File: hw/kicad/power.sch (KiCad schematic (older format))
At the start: 1 part

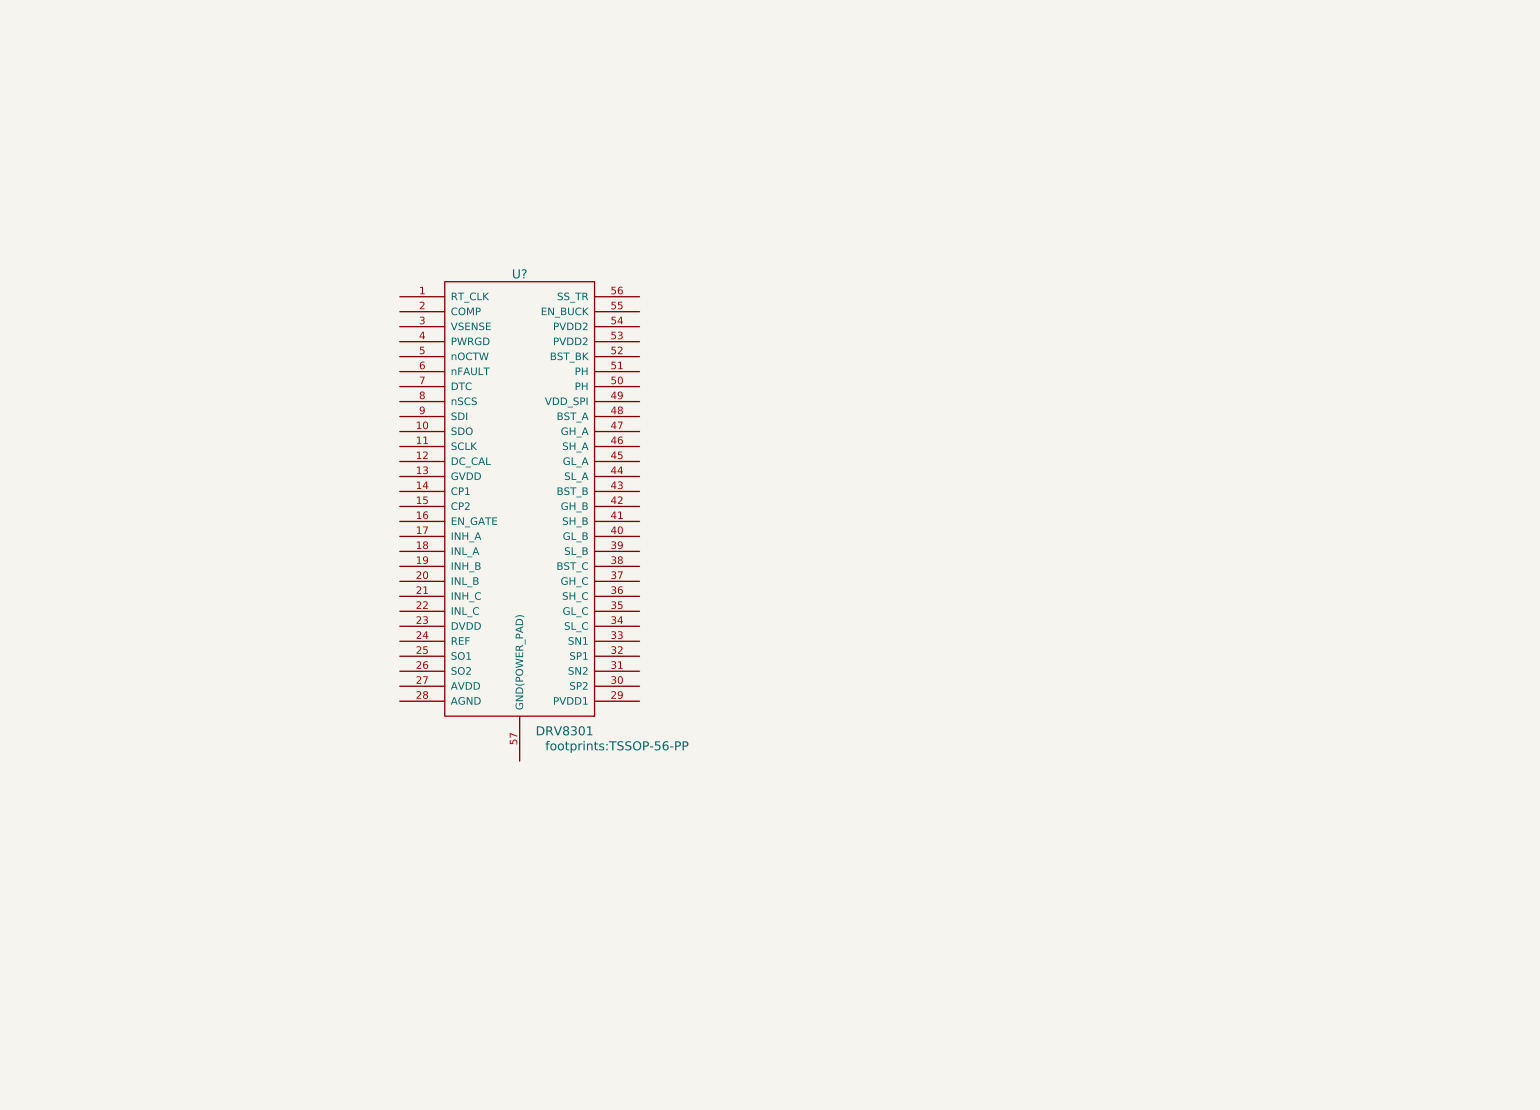
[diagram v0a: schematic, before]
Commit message: First steps on gate driver circuit
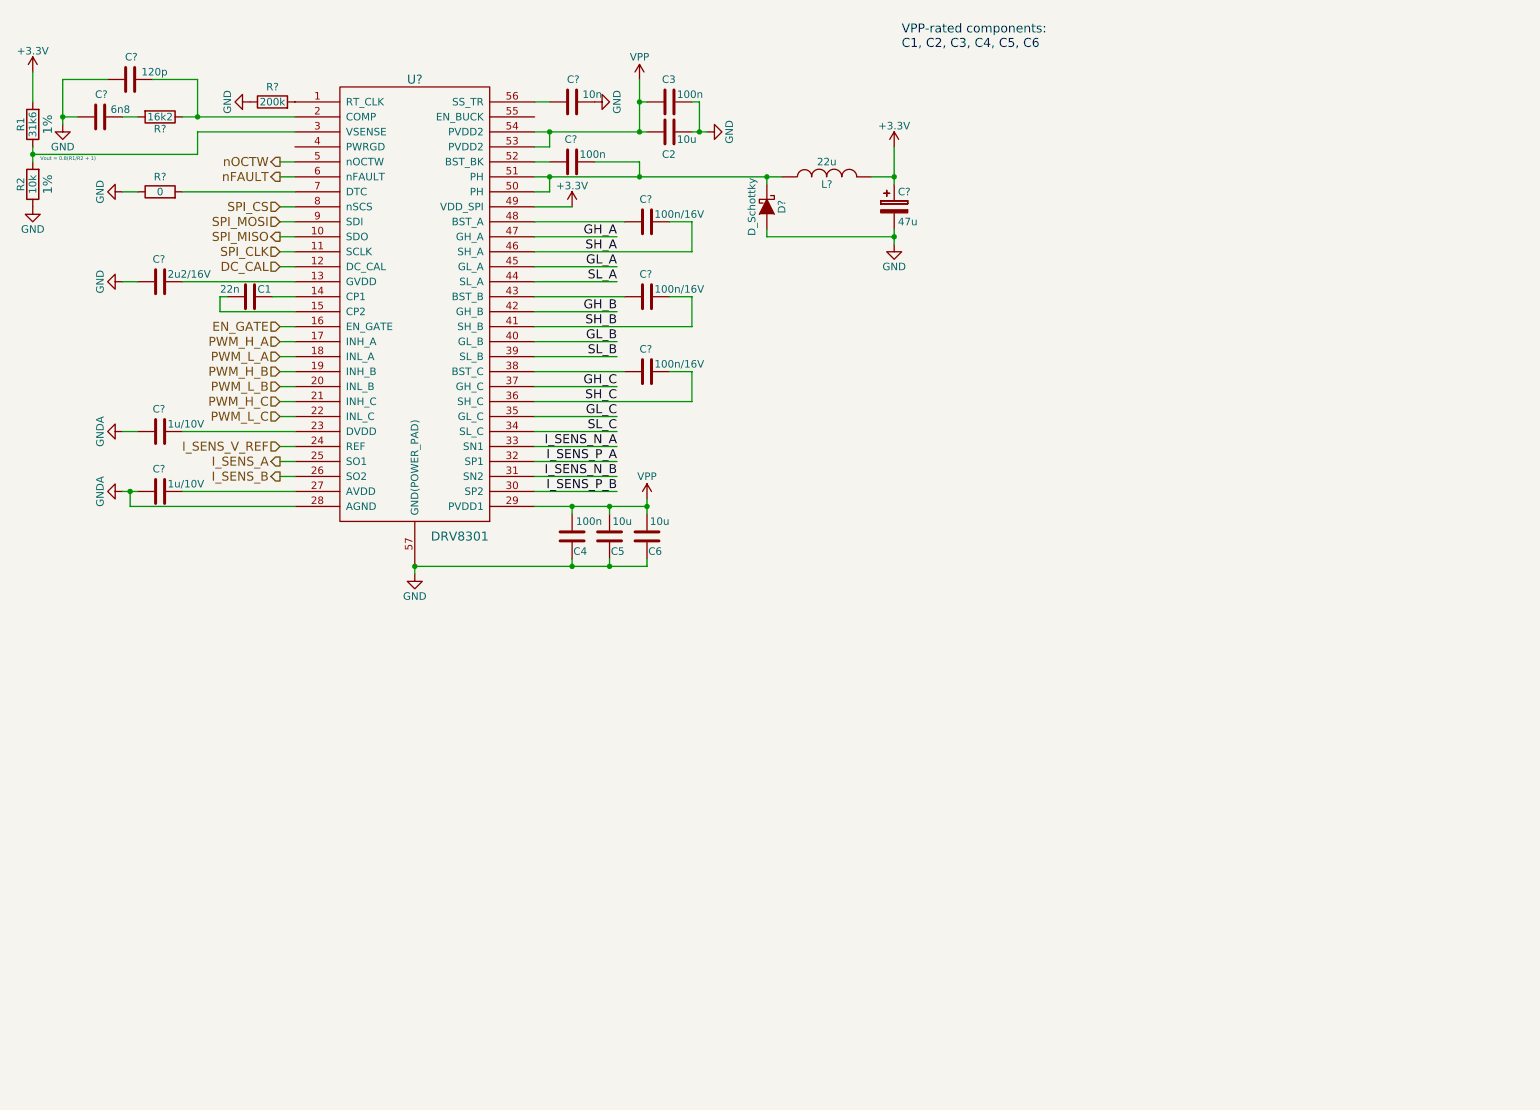
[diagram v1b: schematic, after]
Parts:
- added C1: 22n, symbol C
- added C2, C5, C6: 10u, symbol C
- added C3, C4, C?: 100n, symbol C
- added C?: 10n, symbol C
- added C?: 47u, symbol CP
- added C?: 120p, symbol C
- added C?: 6n8, symbol C
- added C?: 2u2/16V, symbol C
- added C? (x2): 1u/10V, symbol C
- added C? (x3): 100n/16V, symbol C
- added D?: D_Schottky, symbol D_Schottky
- added L?: 22u, symbol INDUCTOR
- added R1: 31k6, symbol R
- added R2: 10k, symbol R
- added R?: 200k, symbol R
- added R?: 16k2, symbol R
- added R?: 0, symbol R
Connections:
- net at U?.1 (RT_CLK): now also R?.2
- net SPI_MISO: now reaches U?.10 (SDO)
- net SPI_CLK: now reaches U?.11 (SCLK)
- net DC_CAL: now reaches U?.12 (DC_CAL)
- net at U?.13 (GVDD): now also C?.1
- net at U?.14 (CP1): now also C1.1
- net at U?.15 (CP2): now also C1.2
- net EN_GATE: now reaches U?.16 (EN_GATE)
- net PWM_H_A: now reaches U?.17 (INH_A)
- net PWM_L_A: now reaches U?.18 (INL_A)
- net PWM_H_B: now reaches U?.19 (INH_B)
- net at U?.2 (COMP): now also C?.2, R?.1
- net PWM_L_B: now reaches U?.20 (INL_B)
- net PWM_H_C: now reaches U?.21 (INH_C)
- net PWM_L_C: now reaches U?.22 (INL_C)
- net at U?.23 (DVDD): now also C?.1
- net I_SENS_V_REF: now reaches U?.24 (REF)
- net I_SENS_A: now reaches U?.25 (SO1)
- net I_SENS_B: now reaches U?.26 (SO2)
- net at U?.27 (AVDD): now also C?.1
- net GNDA: now reaches U?.28 (AGND)
- net GNDA: now also C?.2, C?.2
- net VPP: now reaches U?.29 (PVDD1)
- net VPP: now also U?.53 (PVDD2), U?.54 (PVDD2), C2.2, C3.2, C4.2, C5.2, C6.2
- net at U?.3 (VSENSE): now also R1.1, R2.2
- net I_SENS_P_B: now reaches U?.30 (SP2)
- net I_SENS_N_B: now reaches U?.31 (SN2)
- net I_SENS_P_A: now reaches U?.32 (SP1)
- net I_SENS_N_A: now reaches U?.33 (SN1)
- net SL_C: now reaches U?.34 (SL_C)
- net GL_C: now reaches U?.35 (GL_C)
- net SH_C: now reaches U?.36 (SH_C)
- net SH_C: now also C?.1
- net GH_C: now reaches U?.37 (GH_C)
- net at U?.38 (BST_C): now also C?.2
- net SL_B: now reaches U?.39 (SL_B)
- net GL_B: now reaches U?.40 (GL_B)
- net SH_B: now reaches U?.41 (SH_B)
- net SH_B: now also C?.1
- net GH_B: now reaches U?.42 (GH_B)
- net at U?.43 (BST_B): now also C?.2
- net SL_A: now reaches U?.44 (SL_A)
- net GL_A: now reaches U?.45 (GL_A)
- net SH_A: now reaches U?.46 (SH_A)
- net SH_A: now also C?.1
- net GH_A: now reaches U?.47 (GH_A)
- net at U?.48 (BST_A): now also C?.2
- net +3V3: now reaches U?.49 (VDD_SPI)
- net +3V3: now also C?.1, L?.2, R1.2
- net nOCTW: now reaches U?.5 (nOCTW)
- net at U?.50 (PH): now also U?.51 (PH), C?.1, D?.1 (K), L?.1
- net at U?.52 (BST_BK): now also C?.2
- net at U?.56 (SS_TR): now also C?.1
- net GND: now reaches U?.57 (GND(POWER_PAD))
- net GND: now also C2.1, C3.1, C4.1, C5.1, C6.1, C?.1, C?.1, C?.2, C?.2, C?.2, D?.2 (A), R2.1, R?.1, R?.1
- net nFAULT: now reaches U?.6 (nFAULT)
- net at U?.7 (DTC): now also R?.2
- net SPI_CS: now reaches U?.8 (nSCS)
- net SPI_MOSI: now reaches U?.9 (SDI)
- new net: C?.2, R?.2
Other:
- note added: "VPP-rated components:\nC1, C2, C3, C4, C5, C6"
- note added: "Vout = 0.8(R1/R2 + 1)"
- moved on the sheet: U?

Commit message: Added power mosfet footprint
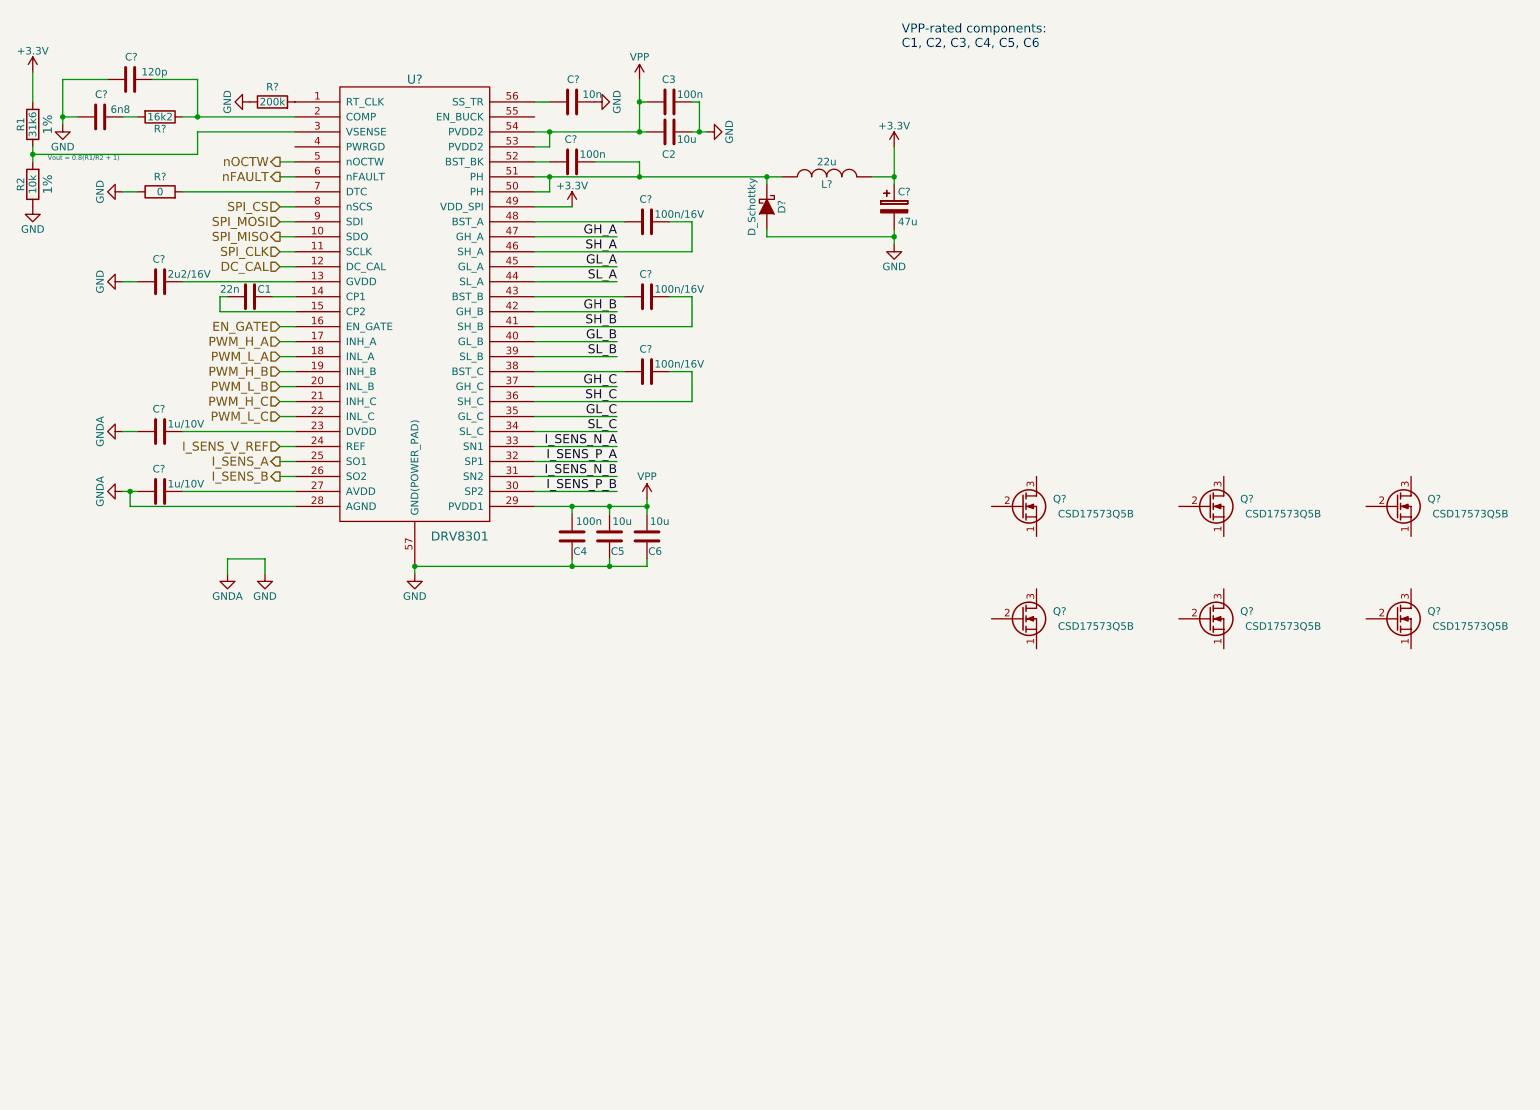
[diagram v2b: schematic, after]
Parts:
- added Q? (x6): CSD17573Q5B, SON_8_5x6:SON_8_5x6, symbol Q_NMOS_SGD
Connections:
- net GNDA is gone; now on net GND: C?.2, C?.2, U?.28 (AGND)
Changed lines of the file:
@@
 	1    0    0    -1
 $EndComp
-Text Notes 950  1500 0    24   ~ 0
+Text Notes 1000 1500 0    31   ~ 0
 Vout = 0.8(R1/R2 + 1)
 $Comp
@@
 Wire Wire Line
 	2650 3600 2550 3600
+$Comp
+L GNDA #PWR?
+U 1 1 581BA227
+P 2200 4250
+F 0 "#PWR?" H 2200 4000 50  0001 C CNN
+F 1 "GNDA" H 2200 4100 50  0000 C CNN
+F 2 "" H 2200 4250 60  0000 C CNN
+F 3 "" H 2200 4250 60  0000 C CNN
+	1    2200 4250
+	1    0    0    -1
+$EndComp
+$Comp
+L GND #PWR?
+U 1 1 581BA296
+P 2450 4250
+F 0 "#PWR?" H 2450 4000 50  0001 C CNN
+F 1 "GND" H 2450 4100 50  0000 C CNN
+F 2 "" H 2450 4250 60  0000 C CNN
+F 3 "" H 2450 4250 60  0000 C CNN
+	1    2450 4250
+	1    0    0    -1
+$EndComp
+Wire Wire Line
+	2450 4250 2450 4150
+Wire Wire Line
+	2450 4150 2200 4150
+Wire Wire Line
+	2200 4150 2200 4250
+$Comp
+L Q_NMOS_SGD Q?
+U 1 1 581CC953
+P 7500 3800
+F 0 "Q?" H 7800 3850 50  0000 R CNN
+F 1 "CSD17573Q5B" H 8250 3750 50  0000 R CNN
+F 2 "SON_8_5x6:SON_8_5x6" H 7700 3900 29  0001 C CNN
+F 3 "" H 7500 3800 60  0000 C CNN
+	1    7500 3800
+	1    0    0    -1
+$EndComp
+$Comp
+L Q_NMOS_SGD Q?
+U 1 1 581CD36C
+P 7500 4550
+F 0 "Q?" H 7800 4600 50  0000 R CNN
+F 1 "CSD17573Q5B" H 8250 4500 50  0000 R CNN
+F 2 "SON_8_5x6:SON_8_5x6" H 7700 4650 29  0001 C CNN
+F 3 "" H 7500 4550 60  0000 C CNN
+	1    7500 4550
+	1    0    0    -1
+$EndComp
+$Comp
+L Q_NMOS_SGD Q?
+U 1 1 581CD3DC
+P 8750 3800
+F 0 "Q?" H 9050 3850 50  0000 R CNN
+F 1 "CSD17573Q5B" H 9500 3750 50  0000 R CNN
+F 2 "SON_8_5x6:SON_8_5x6" H 8950 3900 29  0001 C CNN
+F 3 "" H 8750 3800 60  0000 C CNN
+	1    8750 3800
+	1    0    0    -1
+$EndComp
+$Comp
+L Q_NMOS_SGD Q?
+U 1 1 581CD456
+P 8750 4550
+F 0 "Q?" H 9050 4600 50  0000 R CNN
+F 1 "CSD17573Q5B" H 9500 4500 50  0000 R CNN
+F 2 "SON_8_5x6:SON_8_5x6" H 8950 4650 29  0001 C CNN
+F 3 "" H 8750 4550 60  0000 C CNN
+	1    8750 4550
+	1    0    0    -1
+$EndComp
+$Comp
+L Q_NMOS_SGD Q?
+U 1 1 581CD59A
+P 10000 3800
+F 0 "Q?" H 10300 3850 50  0000 R CNN
+F 1 "CSD17573Q5B" H 10750 3750 50  0000 R CNN
+F 2 "SON_8_5x6:SON_8_5x6" H 10200 3900 29  0001 C CNN
+F 3 "" H 10000 3800 60  0000 C CNN
+	1    10000 3800
+	1    0    0    -1
+$EndComp
+$Comp
+L Q_NMOS_SGD Q?
+U 1 1 581CD612
+P 10000 4550
+F 0 "Q?" H 10300 4600 50  0000 R CNN
+F 1 "CSD17573Q5B" H 10750 4500 50  0000 R CNN
+F 2 "SON_8_5x6:SON_8_5x6" H 10200 4650 29  0001 C CNN
+F 3 "" H 10000 4550 60  0000 C CNN
+	1    10000 4550
+	1    0    0    -1
+$EndComp
 $EndSCHEMATC

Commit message: Some more work on the FET-stage
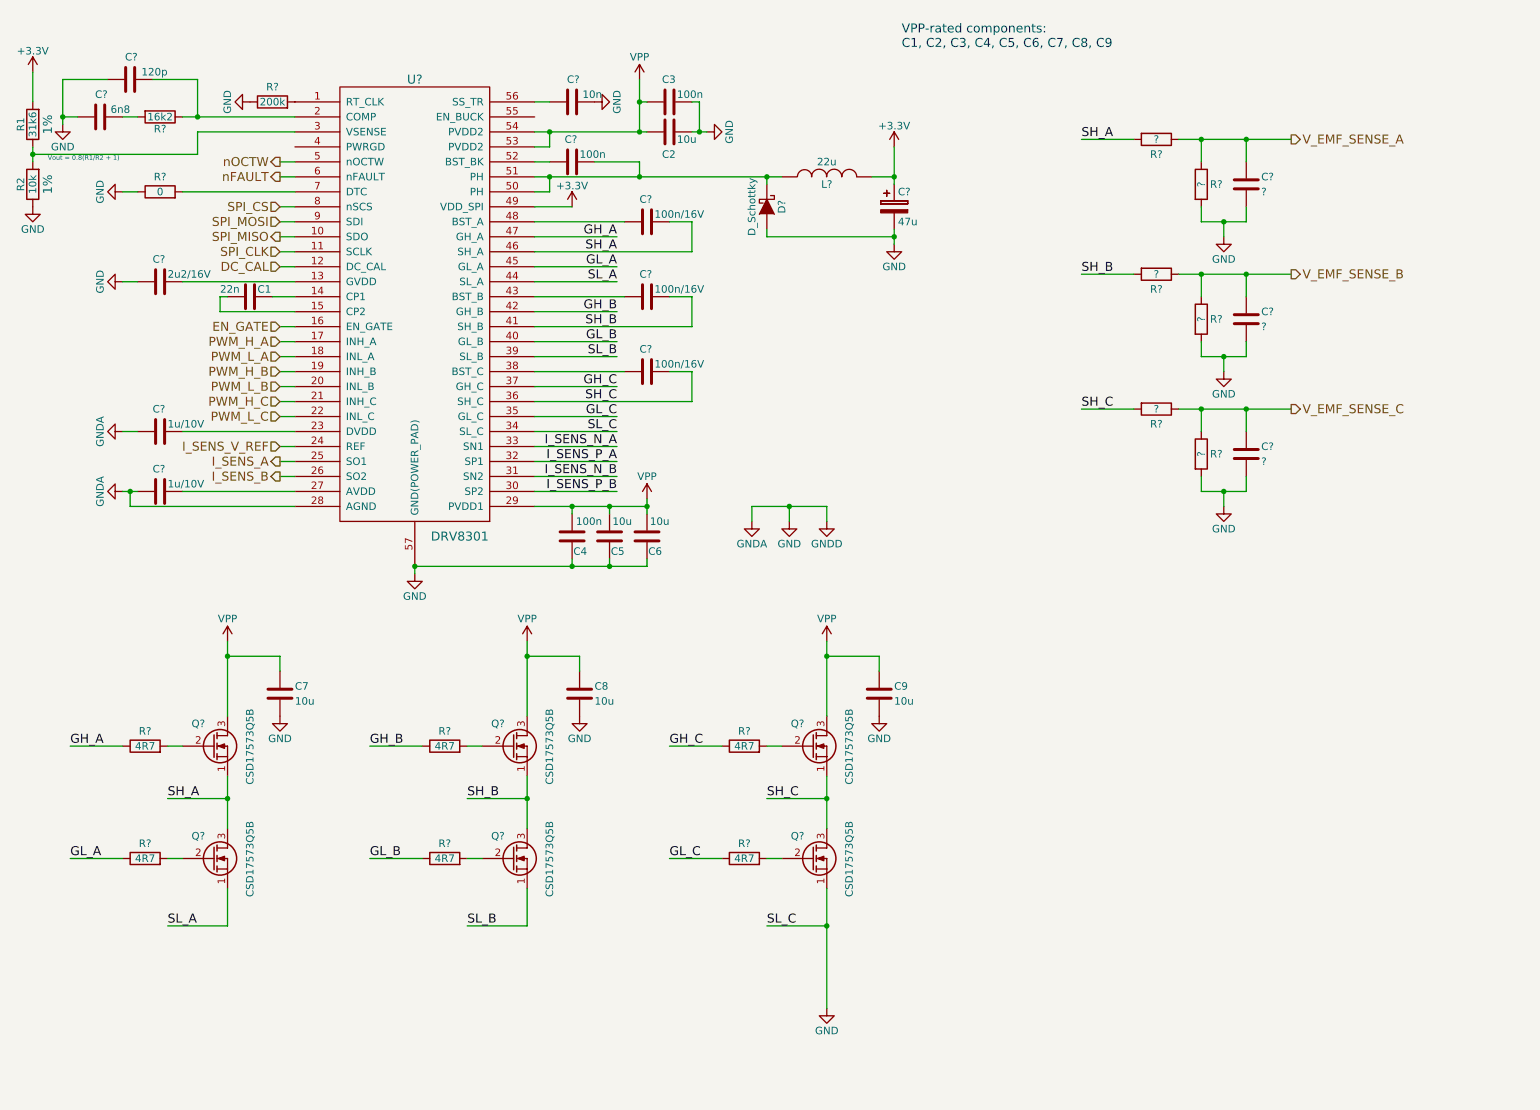
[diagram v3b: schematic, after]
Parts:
- removed Q? (x4): CSD17573Q5B, SON_8_5x6:SON_8_5x6, symbol Q_NMOS_SGD
- added C7, C8, C9: 10u, symbol C
- added C? (x3): ?, symbol C
- added Q? (x4): CSD17573Q5B, SON_8_5x6:SON_8_5x6, symbol Q_NMOS_SGD
- added R? (x6): 4R7, symbol R
- added R? (x6): ?, symbol R
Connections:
- net SL_C is gone; now on net GND: U?.34 (SL_C)
- net GH_A: now also R?.1
- net GH_B: now also R?.1
- net GH_C: now also R?.1
- net GL_A: now also R?.1
- net GL_B: now also R?.1
- net GL_C: now also R?.1
- net GND: now also C7.2, C8.2, C9.2, C?.2, C?.2, C?.2, Q?.1 (S), R?.2, R?.2, R?.2
- net SH_A: now also Q?.1 (S), Q?.3 (D), R?.2
- net SH_B: now also Q?.1 (S), Q?.3 (D), R?.2
- net SH_C: now also Q?.1 (S), Q?.3 (D), R?.2
- net SL_A: now also Q?.1 (S)
- net SL_B: now also Q?.1 (S)
- net VPP: now also Q?.3 (D), C7.1, C8.1, C9.1, Q?.3 (D), Q?.3 (D)
- net at Q?.2 (G): now also R?.2 (x2)
- new net: Q?.2 (G), R?.2 (x4)
- new net V_EMF_SENSE_A: C?.1, R?.1, R?.1
- new net V_EMF_SENSE_B: C?.1, R?.1, R?.1
- new net V_EMF_SENSE_C: C?.1, R?.1, R?.1
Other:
- note added: "VPP-rated components:\nC1, C2, C3, C4, C5, C6, C7, C8, C9"
- note removed: "VPP-rated components:\nC1, C2, C3, C4, C5, C6"
- moved on the sheet: Q?

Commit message: More power work
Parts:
- added C? (x2): 1n, symbol C
- added C?: ?, symbol C
- added R? (x2): WSLP2726 / 2 mOhm, symbol WSLP2726
- added R? (x2): ?, symbol R
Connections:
- net GND: now also C?.2, R?.2, R?.2, R?.2
- net I_SENS_N_A: now also C?.1, R?.3
- net I_SENS_N_B: now also C?.1, R?.3
- net I_SENS_P_A: now also C?.2, R?.4
- net I_SENS_P_B: now also C?.2, R?.4
- net SL_A: now also R?.1
- net SL_B: now also R?.1
- net VPP: now also R?.2
- net SH_A renamed MOT_PH_A
- net SH_B renamed MOT_PH_B
- net SH_C renamed MOT_PH_C
- new net V_BAT_SENSE: C?.1, R?.1, R?.1
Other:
- note added: "Max VPP ≈ 25-30 V"
- note added: "SOx = REF/2 + G * (SPx - SNx)"
- note added: "SPx should connect to the ground side of the \nsense resistor for the best common mode rejection"
- note added: "Total gate drive RMS current ≈ Qg * Nfets * f\nKeep < 30 mA"
- moved on the sheet: C?, R?
